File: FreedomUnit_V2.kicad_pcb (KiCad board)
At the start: 2 copper layers, 80 x 50 mm, 7 parts, among them J3 SMA, J4 USB-C, J5 LCD, M1 Lambda62C-9S, U1 nRF52840

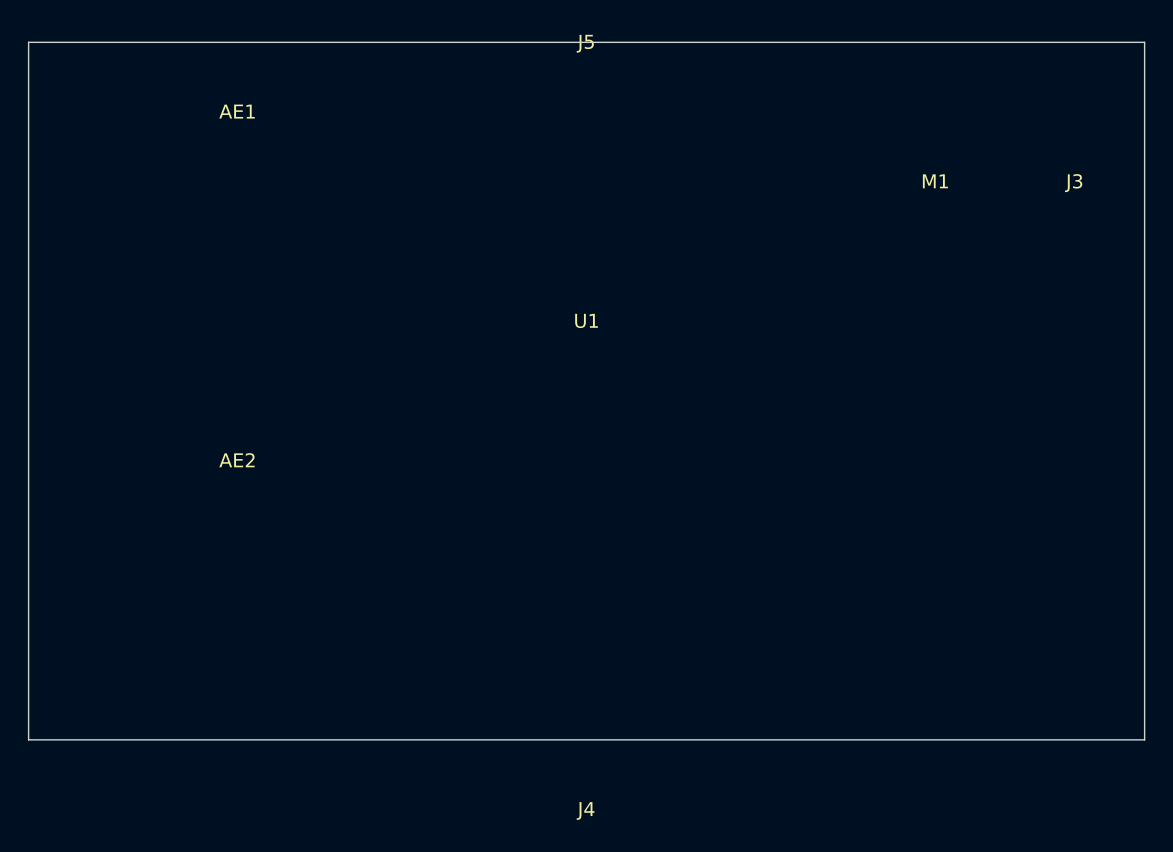
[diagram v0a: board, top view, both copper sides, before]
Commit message: PCB: Partial component placement complete per AI-First Placement Guide
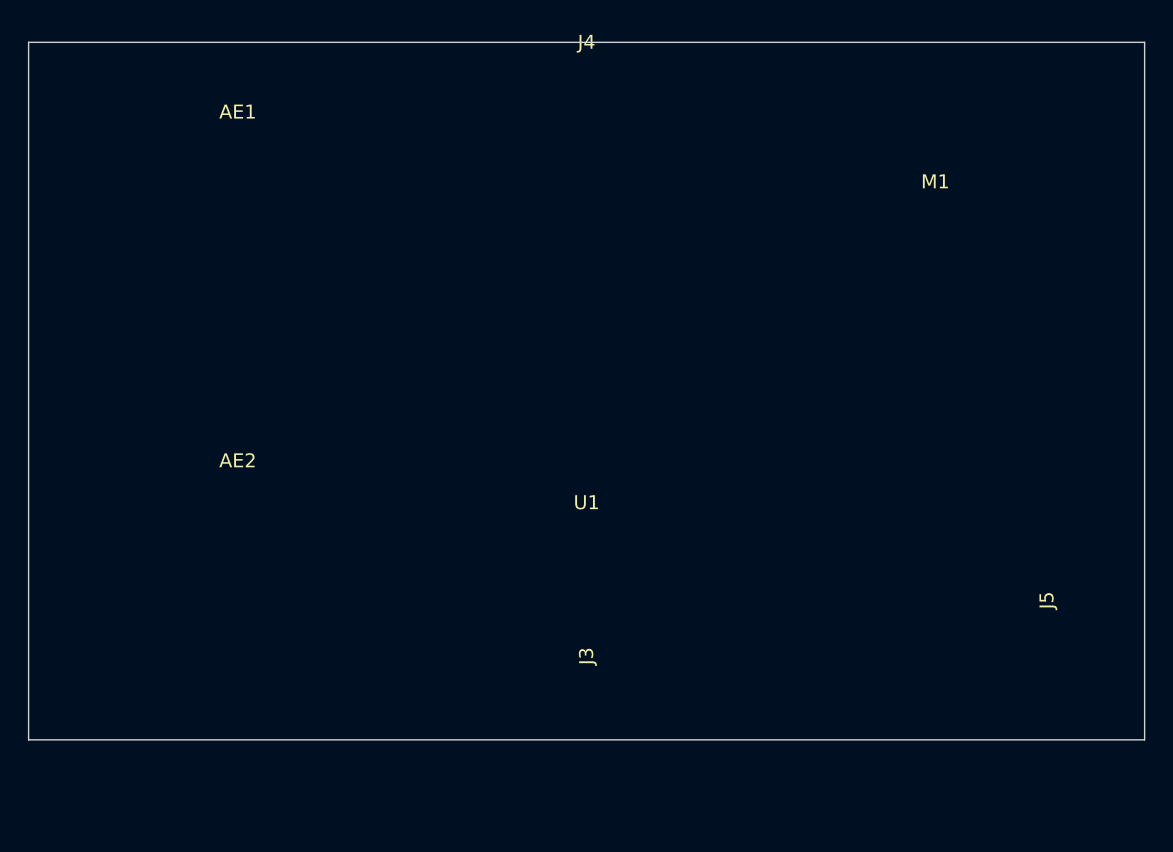
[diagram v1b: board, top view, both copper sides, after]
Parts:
- moved J3 55.9 mm to (40.0, 49.0), turned to 0 degrees
- moved J5 51.7 mm to (78.0, 40.0), turned to 90 degrees
- moved J4 45.0 mm to (40.0, 5.00), turned to 0 degrees
- moved U1 13.0 mm to (40.0, 38.0)
